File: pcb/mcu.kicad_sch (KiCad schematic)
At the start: 26 parts, among them J1 SWD Header, SW1 SKRPABE010, U1 STM32C031G6Ux, Y1 ECS-480-10-37B2-RWN-TR

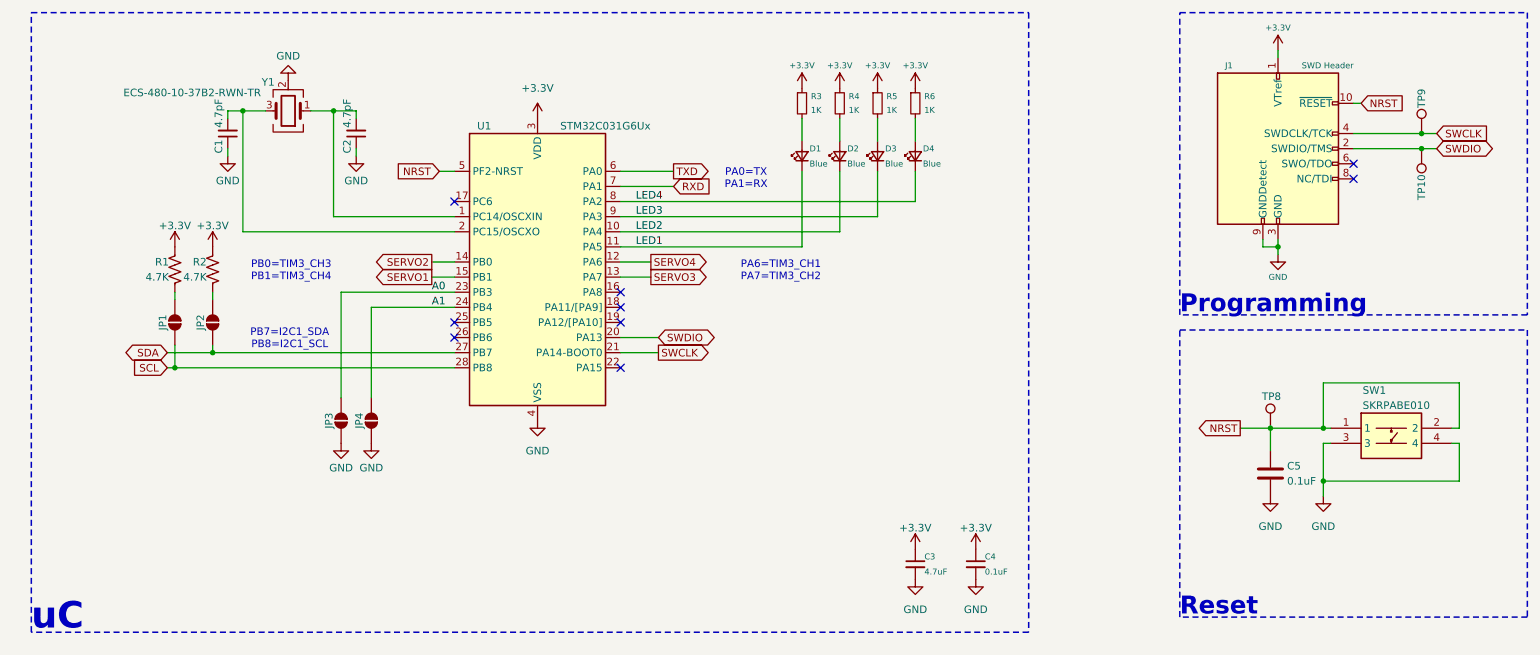
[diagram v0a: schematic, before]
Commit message: Added guard ring
Optimized layout
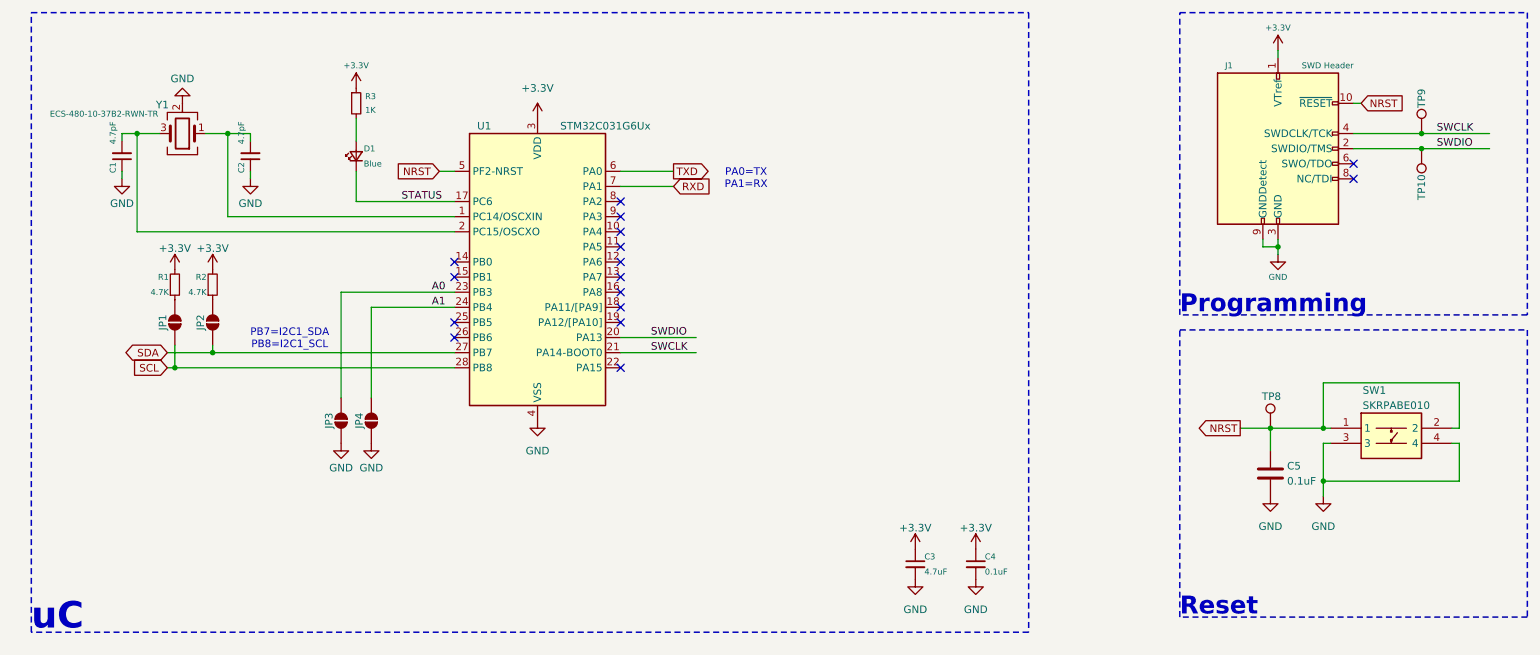
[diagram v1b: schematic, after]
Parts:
- removed D2, D3, D4: Blue, CRGM Passive:LED_0603_1608Metric, symbol Device:LED_Small
- removed R4, R5, R6: 1K, CRGM Passive:R_0603_1608Metric, symbol Device:R_Small
- JP1, JP2, JP3, JP4, TP10, TP8, TP9: value ~ -> (none)
- R1, R2: symbol Device:R_US -> Device:R_Small
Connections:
- net STATUS: now reaches U1.17 (PC6)
- net STATUS: now also D1.1 (K)
- net LED1: no longer names the net of U1.11 (PA5)
- net LED1: no longer D1.1 (K)
- net LED2: no longer names the net of U1.10 (PA4)
- net LED3: no longer names the net of U1.9 (PA3)
- net LED4: no longer names the net of U1.8 (PA2)
- net SERVO1: no longer names the net of U1.15 (PB1)
- net SERVO2: no longer names the net of U1.14 (PB0)
- net SERVO3: no longer names the net of U1.13 (PA7)
- net SERVO4: no longer names the net of U1.12 (PA6)
- no-connect marks 9 -> 16
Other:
- note removed: "PA6=TIM3_CH1 PA7=TIM3_CH2"
- note removed: "PB0=TIM3_CH3 PB1=TIM3_CH4"
- moved on the sheet: C1, C2, D1, R3, Y1
